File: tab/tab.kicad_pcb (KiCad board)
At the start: 2 copper layers, 5 x 19 mm, 9 parts

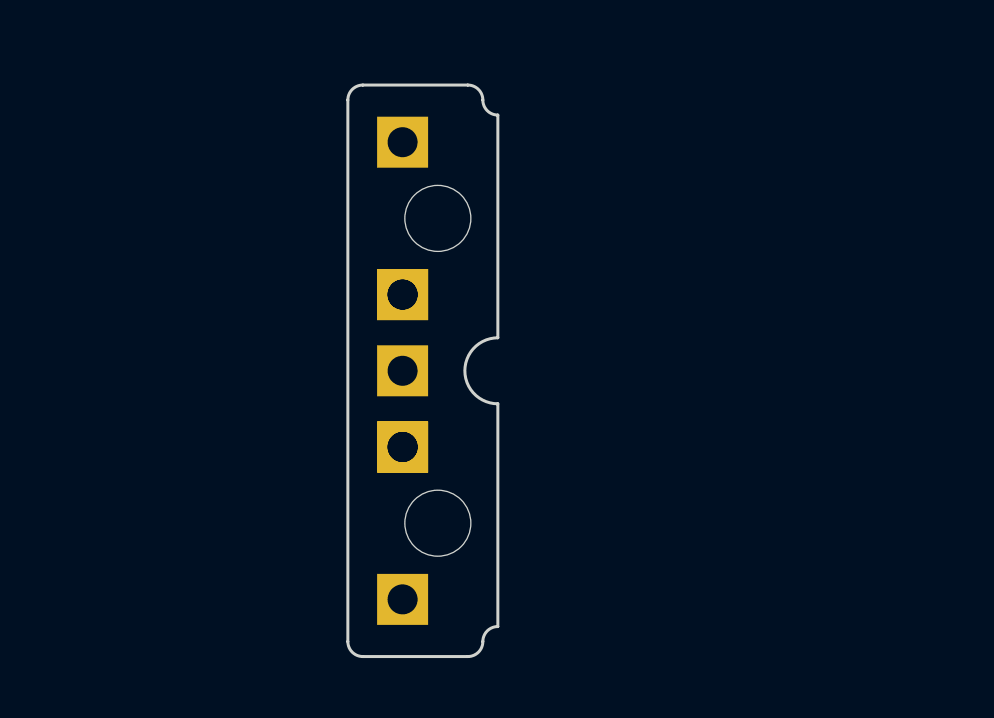
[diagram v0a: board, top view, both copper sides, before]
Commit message: moves GND shorts
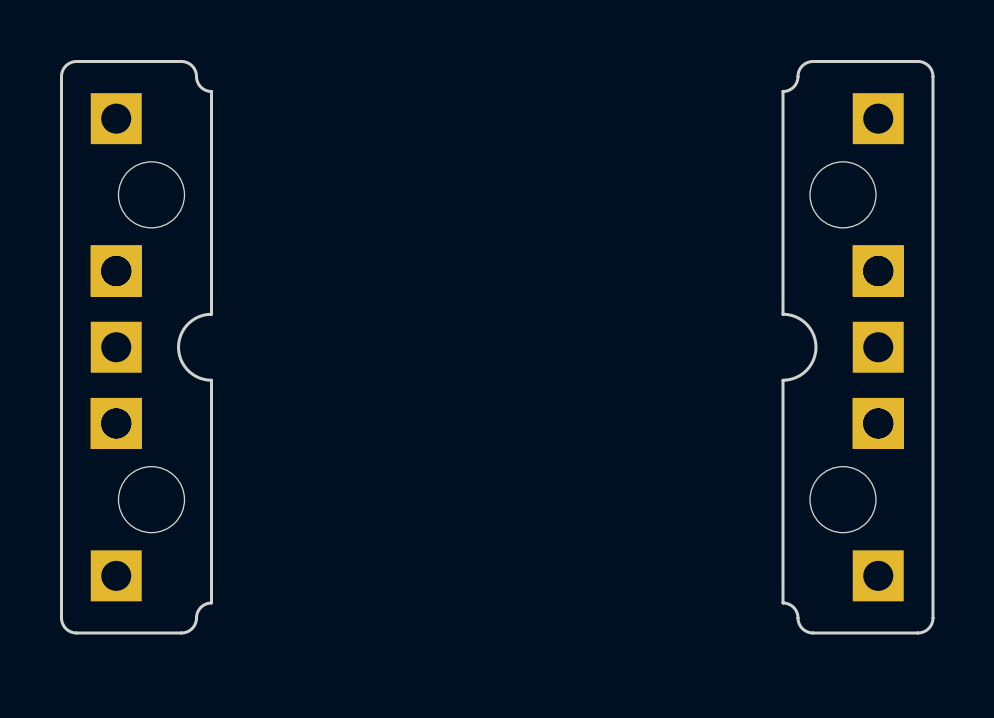
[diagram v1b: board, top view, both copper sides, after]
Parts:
- added ? (x2): , , F.Cu at (106.7, 76.2)
- added ? (x2): , , F.Cu at (106.7, 81.3)
- added ?: , , F.Cu at (106.7, 71.1)
- added ?: , , F.Cu at (106.7, 86.4)
- added ?: , , F.Cu at (106.7, 78.7)
- added H1: MountingHole_2.2mm_M2, MountingHole:MountingHole_2.2mm_M2, F.Cu at (105.5, 83.8)
- added H2: MountingHole_2.2mm_M2, MountingHole:MountingHole_2.2mm_M2, F.Cu at (105.5, 73.7)
- moved ? 9.58 mm to (81.3, 81.3) (x2)
- moved ? 9.58 mm to (81.3, 78.7)
- moved ? 9.58 mm to (81.3, 71.1)
- moved ? 9.58 mm to (81.3, 76.2) (x2)
- moved ? 9.58 mm to (81.3, 86.4)
- moved H1 9.58 mm to (82.5, 73.7)
- moved H2 9.58 mm to (82.5, 83.8)
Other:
- board size 5 x 19 mm -> 29 x 19 mm
- board text added: "Short R1&2 to share GND"

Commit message: changes hole sizes to m1.6
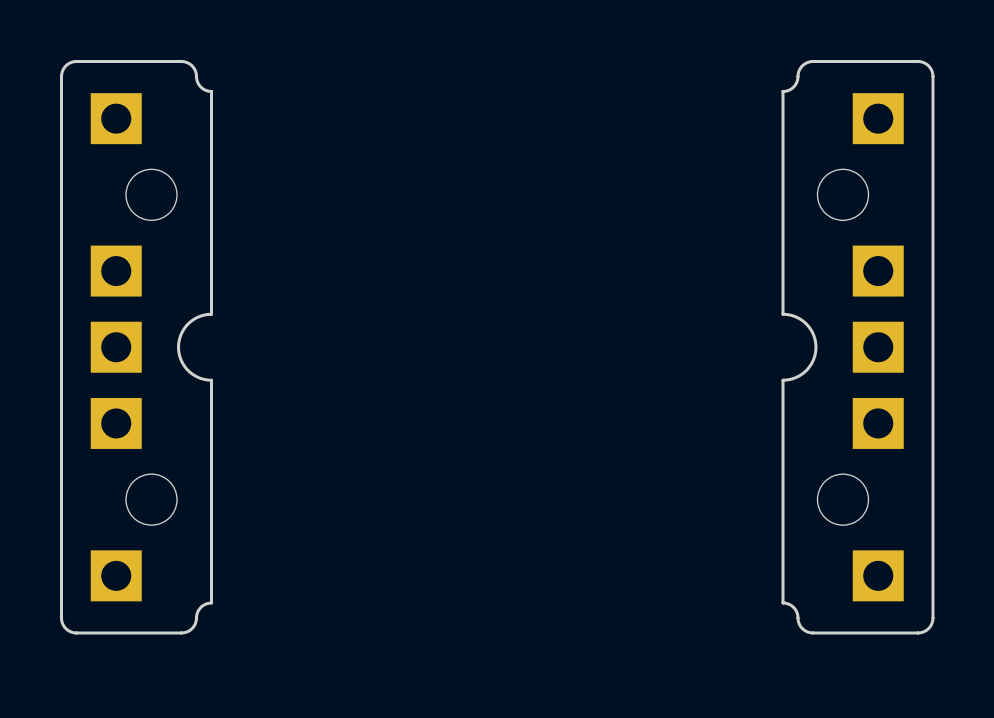
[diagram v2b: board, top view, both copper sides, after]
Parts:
- removed the ? at (81.3, 81.3)
- removed the ? at (106.7, 76.2)
- removed the ? at (106.7, 81.3)
- removed the ? at (81.3, 76.2)
- removed the H1 at (82.5, 73.7)
- removed the H1 at (105.5, 83.8)
- removed the H2 at (82.5, 83.8)
- removed the H2 at (105.5, 73.7)
- added H1: NPTH, PCM_kikit:NPTH, F.Cu at (82.5, 73.7)
- added H2: NPTH, PCM_kikit:NPTH, F.Cu at (82.5, 83.8)
- added H3: NPTH, PCM_kikit:NPTH, F.Cu at (105.5, 73.7)
- added H4: NPTH, PCM_kikit:NPTH, F.Cu at (105.5, 83.8)
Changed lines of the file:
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@@
     (pad "1" thru_hole rect (at 0 0) (size 1.7 1.7) (drill 1) (layers "*.Cu" "*.Mask"))
-  )
-  (footprint "MountingHole:MountingHole_2.2mm_M2" (layer "F.Cu")
-    (at 82.455 83.82 -90)
-    (descr "Mounting Hole 2.2mm, no annular, M2")
-    (tags "mounting hole 2.2mm no annular m2")
-    (attr exclude_from_pos_files exclude_from_bom)
-    (fp_text reference "H2" (at 3.556 0 90) (layer "F.SilkS") hide
-        (effects (font (size 1 1) (thickness 0.15)))
-    )
-    (fp_text value "MountingHole_2.2mm_M2" (at 0 3.2 90) (layer "F.Fab")
-        (effects (font (size 1 1) (thickness 0.15)))
-    )
-    (fp_circle (center 0 0) (end 2 0)
-      (stroke (width 0.05) (type solid)) (fill none) (layer "F.CrtYd"))
-    (pad "" np_thru_hole circle (at 0 0 270) (size 2.2 2.2) (drill 2.2) (layers "*.Cu" "*.Mask"))
   )
   (footprint "" (layer "F.Cu")
@@
     (pad "1" thru_hole rect (at 0 0 180) (size 1.7 1.7) (drill 1) (layers "*.Cu" "*.Mask"))
   )
-  (footprint "MountingHole:MountingHole_2.2mm_M2" (layer "F.Cu")
-    (at 82.455 73.66 -90)
-    (descr "Mounting Hole 2.2mm, no annular, M2")
-    (tags "mounting hole 2.2mm no annular m2")
-    (attr exclude_from_pos_files exclude_from_bom)
-    (fp_text reference "H1" (at 3.556 0 90) (layer "F.SilkS") hide
+  (footprint "PCM_kikit:NPTH" (layer "F.Cu")
+    (at 82.455 73.66)
+    (attr through_hole)
+    (fp_text reference "H1" (at 0 0.5) (layer "F.SilkS") hide
         (effects (font (size 1 1) (thickness 0.15)))
     )
-    (fp_text value "MountingHole_2.2mm_M2" (at 0 3.2 90) (layer "F.Fab")
+    (fp_text value "NPTH" (at 0 -0.5) (layer "F.Fab") hide
         (effects (font (size 1 1) (thickness 0.15)))
     )
-    (fp_circle (center 0 0) (end 2 0)
-      (stroke (width 0.05) (type solid)) (fill none) (layer "F.CrtYd"))
-    (pad "" np_thru_hole circle (at 0 0 270) (size 2.2 2.2) (drill 2.2) (layers "*.Cu" "*.Mask"))
+    (pad "" np_thru_hole circle (at 0 0) (size 1.7 1.7) (drill 1.7) (layers "*.Mask"))
   )
   (footprint "" (layer "F.Cu")
@@
     (pad "1" thru_hole rect (at 0 0) (size 1.7 1.7) (drill 1) (layers "*.Cu" "*.Mask"))
   )
-  (footprint "MountingHole:MountingHole_2.2mm_M2" (layer "F.Cu")
-    (at 105.505 83.82 90)
-    (descr "Mounting Hole 2.2mm, no annular, M2")
-    (tags "mounting hole 2.2mm no annular m2")
-    (attr exclude_from_pos_files exclude_from_bom)
-    (fp_text reference "H1" (at 3.556 0 90) (layer "F.SilkS") hide
-        (effects (font (size 1 1) (thickness 0.15)))
-    )
-    (fp_text value "MountingHole_2.2mm_M2" (at 0 3.2 90) (layer "F.Fab")
-        (effects (font (size 1 1) (thickness 0.15)))
-    )
-    (fp_circle (center 0 0) (end 2 0)
-      (stroke (width 0.05) (type solid)) (fill none) (layer "F.CrtYd"))
-    (pad "" np_thru_hole circle (at 0 0 90) (size 2.2 2.2) (drill 2.2) (layers "*.Cu" "*.Mask"))
-  )
   (footprint "" (layer "F.Cu")
     (at 81.28 86.36 -90)
@@
     (pad "1" thru_hole rect (at 0 0) (size 1.7 1.7) (drill 1) (layers "*.Cu" "*.Mask"))
   )
-  (footprint "" (layer "F.Cu")
-    (at 106.68 81.28 90)
-    (fp_text reference "" (at 0 0 90) (layer "F.SilkS")
-        (effects (font (size 1.27 1.27) (thickness 0.15)))
+  (footprint "PCM_kikit:NPTH" (layer "F.Cu")
+    (at 105.505 73.66)
+    (attr through_hole)
+    (fp_text reference "H3" (at 0 0.5) (layer "F.SilkS") hide
+        (effects (font (size 1 1) (thickness 0.15)))
     )
-    (fp_text value "" (at 0 0 90) (layer "F.SilkS")
-        (effects (font (size 1.27 1.27) (thickness 0.15)))
+    (fp_text value "NPTH" (at 0 -0.5) (layer "F.Fab") hide
+        (effects (font (size 1 1) (thickness 0.15)))
     )
-    (pad "1" thru_hole rect (at 0 0 180) (size 1.7 1.7) (drill 1) (layers "*.Cu" "*.Mask"))
+    (pad "" np_thru_hole circle (at 0 0) (size 1.7 1.7) (drill 1.7) (layers "*.Mask"))
   )
-  (footprint "" (layer "F.Cu")
-    (at 81.28 76.2 -90)
-    (fp_text reference "" (at 0 0 90) (layer "F.SilkS")
-        (effects (font (size 1.27 1.27) (thickness 0.15)))
+  (footprint "PCM_kikit:NPTH" (layer "F.Cu")
+    (at 82.455 83.82)
+    (attr through_hole)
+    (fp_text reference "H2" (at 0 0.5) (layer "F.SilkS") hide
+        (effects (font (size 1 1) (thickness 0.15)))
     )
-    (fp_text value "" (at 0 0 90) (layer "F.SilkS")
-        (effects (font (size 1.27 1.27) (thickness 0.15)))
+    (fp_text value "NPTH" (at 0 -0.5) (layer "F.Fab") hide
+        (effects (font (size 1 1) (thickness 0.15)))
     )
-    (pad "1" thru_hole rect (at 0 0) (size 1.7 1.7) (drill 1) (layers "*.Cu" "*.Mask"))
+    (pad "" np_thru_hole circle (at 0 0) (size 1.7 1.7) (drill 1.7) (layers "*.Mask"))
+  )
+  (footprint "PCM_kikit:NPTH" (layer "F.Cu")
+    (at 105.505 83.82)
+    (attr through_hole)
+    (fp_text reference "H4" (at 0 0.5) (layer "F.SilkS") hide
+        (effects (font (size 1 1) (thickness 0.15)))
+    )
+    (fp_text value "NPTH" (at 0 -0.5) (layer "F.Fab") hide
+        (effects (font (size 1 1) (thickness 0.15)))
+    )
+    (pad "" np_thru_hole circle (at 0 0) (size 1.7 1.7) (drill 1.7) (layers "*.Mask"))
   )
   (footprint "" (layer "F.Cu")
@@
     (pad "1" thru_hole rect (at 0 0) (size 1.7 1.7) (drill 1) (layers "*.Cu" "*.Mask"))
   )
-  (footprint "MountingHole:MountingHole_2.2mm_M2" (layer "F.Cu")
-    (at 105.505 73.66 90)
-    (descr "Mounting Hole 2.2mm, no annular, M2")
-    (tags "mounting hole 2.2mm no annular m2")
-    (attr exclude_from_pos_files exclude_from_bom)
-    (fp_text reference "H2" (at 3.556 0 90) (layer "F.SilkS") hide
-        (effects (font (size 1 1) (thickness 0.15)))
-    )
-    (fp_text value "MountingHole_2.2mm_M2" (at 0 3.2 90) (layer "F.Fab")
-        (effects (font (size 1 1) (thickness 0.15)))
-    )
-    (fp_circle (center 0 0) (end 2 0)
-      (stroke (width 0.05) (type solid)) (fill none) (layer "F.CrtYd"))
-    (pad "" np_thru_hole circle (at 0 0 90) (size 2.2 2.2) (drill 2.2) (layers "*.Cu" "*.Mask"))
-  )
   (footprint "" (layer "F.Cu")
     (at 106.68 76.2 90)
@@
         (effects (font (size 1.27 1.27) (thickness 0.15)))
     )
-    (pad "1" thru_hole rect (at 0 0 180) (size 1.7 1.7) (drill 1) (layers "*.Cu" "*.Mask"))
-  )
-  (footprint "" (layer "F.Cu")
-    (at 81.28 81.28)
-    (fp_text reference "" (at 0 0) (layer "F.SilkS")
-        (effects (font (size 1.27 1.27) (thickness 0.15)))
-    )
-    (fp_text value "" (at 0 0) (layer "F.SilkS")
-        (effects (font (size 1.27 1.27) (thickness 0.15)))
-    )
-    (pad "1" thru_hole rect (at 0 0) (size 1.7 1.7) (drill 1) (layers "*.Cu" "*.Mask"))
-  )
-  (footprint "" (layer "F.Cu")
-    (at 106.68 76.2 180)
-    (fp_text reference "" (at 0 0) (layer "F.SilkS")
-        (effects (font (size 1.27 1.27) (thickness 0.15)))
-    )
-    (fp_text value "" (at 0 0) (layer "F.SilkS")
-        (effects (font (size 1.27 1.27) (thickness 0.15)))
-    )
